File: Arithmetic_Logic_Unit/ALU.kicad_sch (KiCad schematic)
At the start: 32 parts, among them U10 74LS245, U11 74LS173, U4 74LS08, U5 74LS86, U6 74LS86, U7 74LS02, U8 74LS283, U9 74LS283

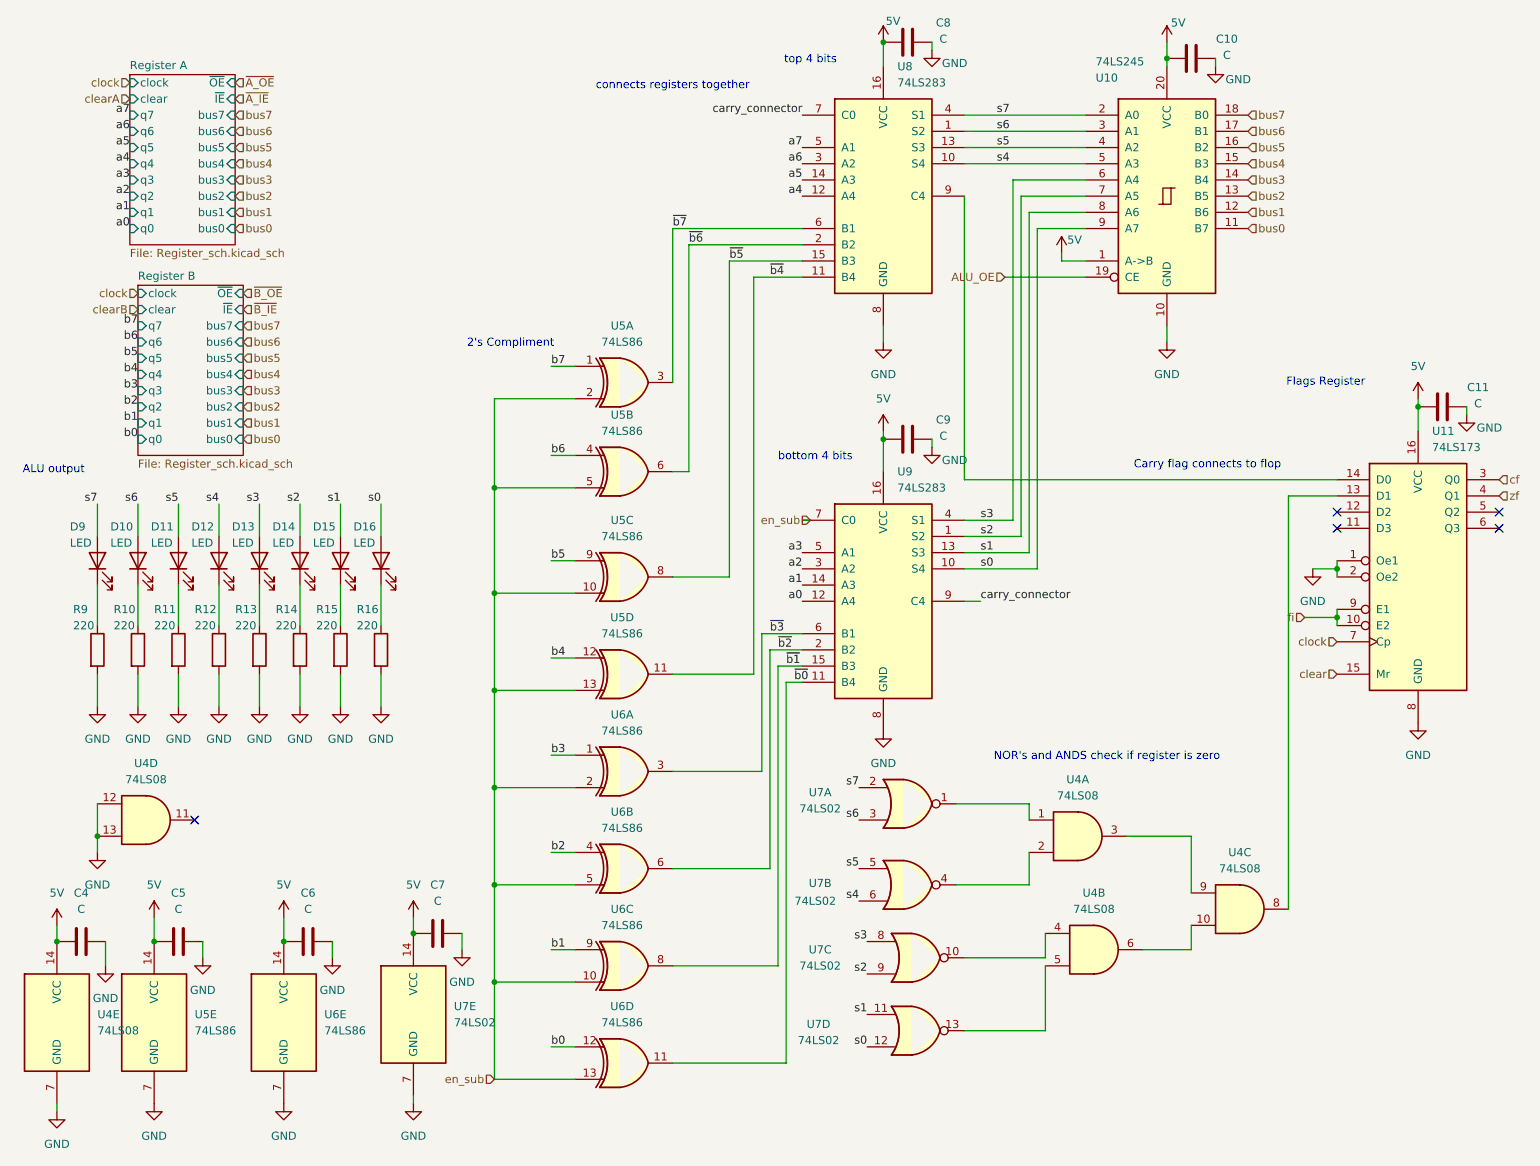
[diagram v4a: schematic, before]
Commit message: preliminary board layout, will move IR to clock module
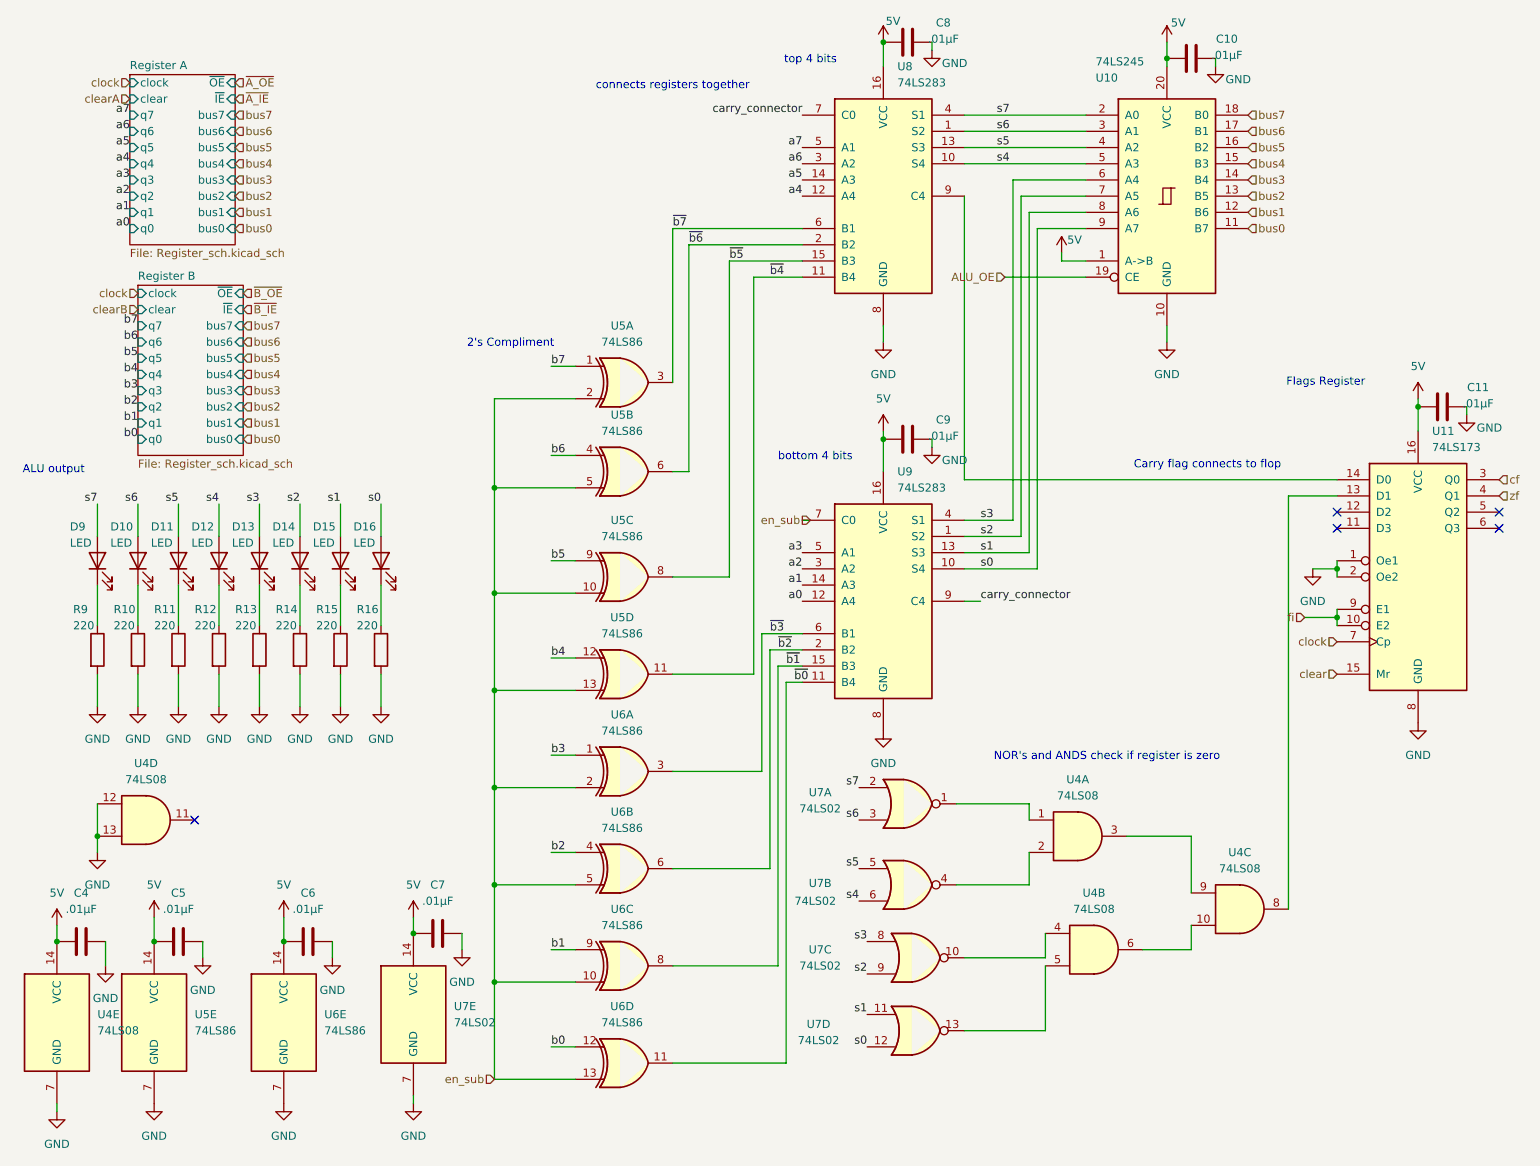
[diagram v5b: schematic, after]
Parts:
- C10, C11, C4, C5, C6, C7, C8, C9: value C -> .01µF; footprint (none) -> Capacitor_THT:C_Disc_D5.0mm_W2.5mm_P2.50mm
- D10, D11, D12, D13, D14, D15, D16, D9: footprint (none) -> LED_THT:LED_D5.0mm
- R10, R11, R12, R13, R14, R15, R16, R9: footprint (none) -> Resistor_THT:R_Axial_DIN0207_L6.3mm_D2.5mm_P5.08mm_Vertical
- U10: footprint (none) -> Package_DIP:DIP-20_W7.62mm
- U11, U8, U9: footprint (none) -> Package_DIP:DIP-16_W7.62mm
- U4, U5, U6, U7: footprint (none) -> Package_DIP:DIP-14_W7.62mm
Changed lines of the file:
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@@
 			)
 		)
-		(property "Footprint" ""
+		(property "Footprint" "LED_THT:LED_D5.0mm"
 			(at 63.5 97.79 0)
 			(effects
@@
 			)
 		)
-		(property "Footprint" ""
+		(property "Footprint" "Package_DIP:DIP-14_W7.62mm"
 			(at 181.61 158.75 0)
 			(effects
@@
 			)
 		)
-		(property "Footprint" ""
+		(property "Footprint" "Package_DIP:DIP-14_W7.62mm"
 			(at 107.95 69.85 0)
 			(effects
@@
 			)
 		)
-		(property "Value" "C"
+		(property "Value" ".01µF"
 			(at 22.86 152.4 90)
 			(effects
@@
 			)
 		)
-		(property "Footprint" ""
+		(property "Footprint" "Capacitor_THT:C_Disc_D5.0mm_W2.5mm_P2.50mm"
 			(at 19.05 158.4452 0)
 			(effects
@@
 			)
 		)
-		(property "Footprint" ""
+		(property "Footprint" "Package_DIP:DIP-14_W7.62mm"
 			(at 107.95 100.33 0)
 			(effects
@@
 			)
 		)
-		(property "Value" "C"
+		(property "Value" ".01µF"
 			(at 157.988 16.002 90)
 			(effects
@@
 			)
 		)
-		(property "Footprint" ""
+		(property "Footprint" "Capacitor_THT:C_Disc_D5.0mm_W2.5mm_P2.50mm"
 			(at 148.59 17.4752 0)
 			(effects
@@
 			)
 		)
-		(property "Footprint" ""
+		(property "Footprint" "Package_DIP:DIP-16_W7.62mm"
 			(at 148.59 40.64 0)
 			(effects
@@
 			)
 		)
-		(property "Footprint" ""
+		(property "Footprint" "Package_DIP:DIP-14_W7.62mm"
 			(at 54.61 170.18 0)
 			(effects
@@
 			)
 		)
-		(property "Footprint" ""
+		(property "Footprint" "Package_DIP:DIP-14_W7.62mm"
 			(at 107.95 83.82 0)
 			(effects
@@
 			)
 		)
-		(property "Footprint" ""
+		(property "Footprint" "Package_DIP:DIP-14_W7.62mm"
 			(at 107.95 176.53 0)
 			(effects
@@
 			)
 		)
-		(property "Footprint" ""
+		(property "Footprint" "LED_THT:LED_D5.0mm"
 			(at 44.45 97.79 0)
 			(effects
@@
 			)
 		)
-		(property "Footprint" ""
+		(property "Footprint" "Resistor_THT:R_Axial_DIN0207_L6.3mm_D2.5mm_P5.08mm_Vertical"
 			(at 23.622 111.76 90)
 			(effects
@@
 			)
 		)
-		(property "Value" "C"
+		(property "Value" ".01µF"
 			(at 78.74 151.13 90)
 			(effects
@@
 			)
 		)
-		(property "Footprint" ""
+		(property "Footprint" "Capacitor_THT:C_Disc_D5.0mm_W2.5mm_P2.50mm"
 			(at 74.93 157.1752 0)
 			(effects
@@
 			)
 		)
-		(property "Footprint" ""
+		(property "Footprint" "Package_DIP:DIP-14_W7.62mm"
 			(at 107.95 146.05 0)
 			(effects
@@
 			)
 		)
-		(property "Footprint" ""
+		(property "Footprint" "Resistor_THT:R_Axial_DIN0207_L6.3mm_D2.5mm_P5.08mm_Vertical"
 			(at 61.722 111.76 90)
 			(effects
@@
 			)
 		)
-		(property "Value" "C"
+		(property "Value" ".01µF"
 			(at 241.808 73.152 90)
 			(effects
@@
 			)
 		)
-		(property "Footprint" ""
+		(property "Footprint" "Capacitor_THT:C_Disc_D5.0mm_W2.5mm_P2.50mm"
 			(at 232.41 74.6252 0)
 			(effects
@@
 			)
 		)
-		(property "Footprint" ""
+		(property "Footprint" "Package_DIP:DIP-20_W7.62mm"
 			(at 193.04 40.64 0)
 			(effects
@@
 			)
 		)
-		(property "Footprint" ""
+		(property "Footprint" "Package_DIP:DIP-14_W7.62mm"
 			(at 74.93 168.91 0)
 			(effects
@@
 			)
 		)
-		(property "Footprint" ""
+		(property "Footprint" "LED_THT:LED_D5.0mm"
 			(at 25.4 97.79 0)
 			(effects
@@
 			)
 		)
-		(property "Value" "C"
+		(property "Value" ".01µF"
 			(at 202.438 18.542 90)
 			(effects
@@
 			)
 		)
-		(property "Footprint" ""
+		(property "Footprint" "Capacitor_THT:C_Disc_D5.0mm_W2.5mm_P2.50mm"
 			(at 193.04 20.0152 0)
 			(effects
@@
 			)
 		)
-		(property "Footprint" ""
+		(property "Footprint" "Package_DIP:DIP-14_W7.62mm"
 			(at 152.4 135.89 0)
 			(effects
@@
 			)
 		)
-		(property "Footprint" ""
+		(property "Footprint" "Package_DIP:DIP-14_W7.62mm"
 			(at 34.29 170.18 0)
 			(effects
@@
 			)
 		)
-		(property "Footprint" ""
+		(property "Footprint" "Resistor_THT:R_Axial_DIN0207_L6.3mm_D2.5mm_P5.08mm_Vertical"
 			(at 55.372 111.76 90)
 			(effects
@@
 			)
 		)
-		(property "Footprint" ""
+		(property "Footprint" "Resistor_THT:R_Axial_DIN0207_L6.3mm_D2.5mm_P5.08mm_Vertical"
 			(at 36.322 111.76 90)
 			(effects
@@
 			)
 		)
-		(property "Footprint" ""
+		(property "Footprint" "Package_DIP:DIP-14_W7.62mm"
 			(at 107.95 130.81 0)
 			(effects
@@
 			)
 		)
-		(property "Footprint" ""
+		(property "Footprint" "Package_DIP:DIP-14_W7.62mm"
 			(at 107.95 161.29 0)
 			(effects
@@
 			)
 		)
-		(property "Footprint" ""
+		(property "Footprint" "Resistor_THT:R_Axial_DIN0207_L6.3mm_D2.5mm_P5.08mm_Vertical"
 			(at 49.022 111.76 90)
 			(effects
@@
 			)
 		)
-		(property "Footprint" ""
+		(property "Footprint" "Package_DIP:DIP-14_W7.62mm"
 			(at 153.67 160.02 0)
 			(effects
@@
 			)
 		)
-		(property "Footprint" ""
+		(property "Footprint" "Package_DIP:DIP-16_W7.62mm"
 			(at 148.59 104.14 0)
 			(effects
@@
 			)
 		)
-		(property "Footprint" ""
+		(property "Footprint" "LED_THT:LED_D5.0mm"
 			(at 50.8 97.79 0)
 			(effects
@@
 			)
 		)
-		(property "Value" "C"
+		(property "Value" ".01µF"
 			(at 157.988 78.232 90)
 			(effects
@@
 			)
 		)
-		(property "Footprint" ""
+		(property "Footprint" "Capacitor_THT:C_Disc_D5.0mm_W2.5mm_P2.50mm"
 			(at 148.59 79.7052 0)
 			(effects
@@
 			)
 		)
-		(property "Footprint" ""
+		(property "Footprint" "Resistor_THT:R_Axial_DIN0207_L6.3mm_D2.5mm_P5.08mm_Vertical"
 			(at 68.072 111.76 90)
 			(effects
@@
 			)
 		)
-		(property "Footprint" ""
+		(property "Footprint" "Package_DIP:DIP-14_W7.62mm"
 			(at 19.05 170.18 0)
 			(effects
@@
 			)
 		)
-		(property "Footprint" ""
+		(property "Footprint" "Package_DIP:DIP-14_W7.62mm"
 			(at 152.4 148.59 0)
 			(effects
@@
 			)
 		)
-		(property "Footprint" ""
+		(property "Footprint" "Package_DIP:DIP-14_W7.62mm"
 			(at 179.07 140.97 0)
 			(effects
@@
 			)
 		)
-		(property "Footprint" ""
+		(property "Footprint" "Package_DIP:DIP-14_W7.62mm"
 			(at 33.02 138.43 0)
 			(effects
@@
 			)
 		)
-		(property "Footprint" ""
+		(property "Footprint" "Resistor_THT:R_Axial_DIN0207_L6.3mm_D2.5mm_P5.08mm_Vertical"
 			(at 29.972 111.76 90)
 			(effects
@@
 			)
 		)
-		(property "Footprint" ""
+		(property "Footprint" "LED_THT:LED_D5.0mm"
 			(at 38.1 97.79 0)
 			(effects
@@
 			)
 		)
-		(property "Footprint" ""
+		(property "Footprint" "Package_DIP:DIP-14_W7.62mm"
 			(at 153.67 171.45 0)
 			(effects
@@
 			)
 		)
-		(property "Value" "C"
+		(property "Value" ".01µF"
 			(at 58.42 152.4 90)
 			(effects
@@
 			)
 		)
-		(property "Footprint" ""
+		(property "Footprint" "Capacitor_THT:C_Disc_D5.0mm_W2.5mm_P2.50mm"
 			(at 54.61 158.4452 0)
 			(effects
@@
 			)
 		)
-		(property "Footprint" ""
+		(property "Footprint" "Package_DIP:DIP-16_W7.62mm"
 			(at 232.41 100.33 0)
 			(effects
@@
 			)
 		)
-		(property "Footprint" ""
+		(property "Footprint" "LED_THT:LED_D5.0mm"
 			(at 69.85 97.79 0)
 			(effects
@@
 			)
 		)
-		(property "Footprint" ""
+		(property "Footprint" "Resistor_THT:R_Axial_DIN0207_L6.3mm_D2.5mm_P5.08mm_Vertical"
 			(at 42.672 111.76 90)
 			(effects
@@
 			)
 		)
-		(property "Footprint" ""
+		(property "Footprint" "LED_THT:LED_D5.0mm"
 			(at 57.15 97.79 0)
 			(effects
@@
 			)
 		)
-		(property "Footprint" ""
+		(property "Footprint" "Package_DIP:DIP-14_W7.62mm"
 			(at 107.95 115.57 0)
 			(effects
@@
 			)
 		)
-		(property "Footprint" ""
+		(property "Footprint" "LED_THT:LED_D5.0mm"
 			(at 31.75 97.79 0)
 			(effects
@@
 			)
 		)
-		(property "Footprint" ""
+		(property "Footprint" "Package_DIP:DIP-14_W7.62mm"
 			(at 204.47 152.4 0)
 			(effects
@@
 			)
 		)
-		(property "Value" "C"
+		(property "Value" ".01µF"
 			(at 38.1 152.4 90)
 			(effects
@@
 			)
 		)
-		(property "Footprint" ""
+		(property "Footprint" "Capacitor_THT:C_Disc_D5.0mm_W2.5mm_P2.50mm"
 			(at 34.29 158.4452 0)
 			(effects

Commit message: layed out PCB
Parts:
- renumbered D15 to D10, D14 to D11, D13 to D12, D12 to D13, D11 to D14, D10 to D15, D9 to D16, D16 to D9, R15 to R10, R14 to R11, R13 to R12, R12 to R13, R11 to R14, R10 to R15, R9 to R16, R16 to R9
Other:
- moved on the sheet: D10, D11, D12, D13, D14, D15, D16, D9, R10, R11, R12, R13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

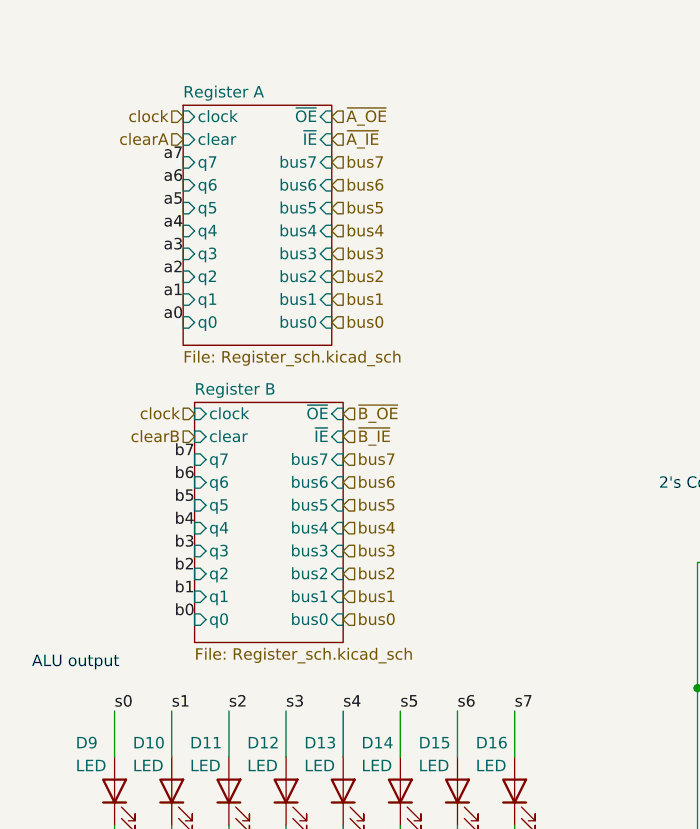
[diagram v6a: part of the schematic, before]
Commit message: Placed clock module again
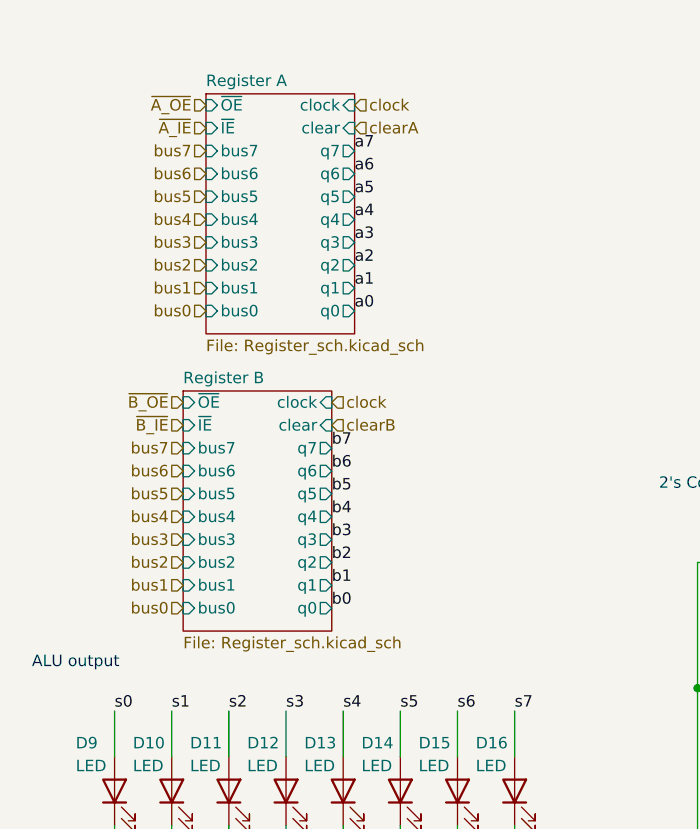
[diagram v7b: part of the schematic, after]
